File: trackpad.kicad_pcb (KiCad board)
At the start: 2 copper layers, 172 x 152.9 mm, 102 parts, among them J1 USB_C_Receptacle_USB2.0, J10 Conn_01x01_Pin, J3 Conn_01x03, J5 Conn_01x07_Pin, J6 Conn_01x04_Pin, J7 Conn_01x02_Pin, J8 Conn_01x08_Pin, J9 Conn_01x02_Pin, SW1 RotaryEncoder_Switch, SW2 SW_Push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

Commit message: Cleanup
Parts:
- removed R16: 0k, Resistor_SMD:R_0402_1005Metric_Pad0.72x0.64mm_HandSolder
- JP1: footprint Jumper:SolderJumper-3_P1.3mm_Open_RoundedPad1.0x1.5mm -> Jumper:SolderJumper-3_P1.3mm_Bridged2Bar12_RoundedPad1.0x1.5mm
- moved R12 0.66 mm to (95.8, 167.6)
- moved C39 0.19 mm to (96.8, 179.0)
- moved C28 0.19 mm to (100.5, 176.3)
- moved U5 0.15 mm to (98.0, 176.8)
- moved J10 0.14 mm to (101.6, 178.3)
- moved C19 0.12 mm to (108.3, 164.6)
- moved C21 0.12 mm to (108.6, 173.4)
- moved C18 0.11 mm to (108.3, 163.7)
- moved C20 0.10 mm to (107.7, 173.4)
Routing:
- net /Sensor/Shield: track 664.8 -> 672.5 mm
- net VCC: track 87.8 -> 86.3 mm
- net +3V3: track 89.7 -> 88.5 mm
- net Net-(U4-TEST): track 6.34 -> 5.79 mm
- net GND2: track 65.1 -> 65.4 mm, vias 72 -> 71
- net GND: vias 60 -> 63
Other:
- board text added: "RESET"
- board text removed: "Remove R16 first!"
- board text removed: "Reset"

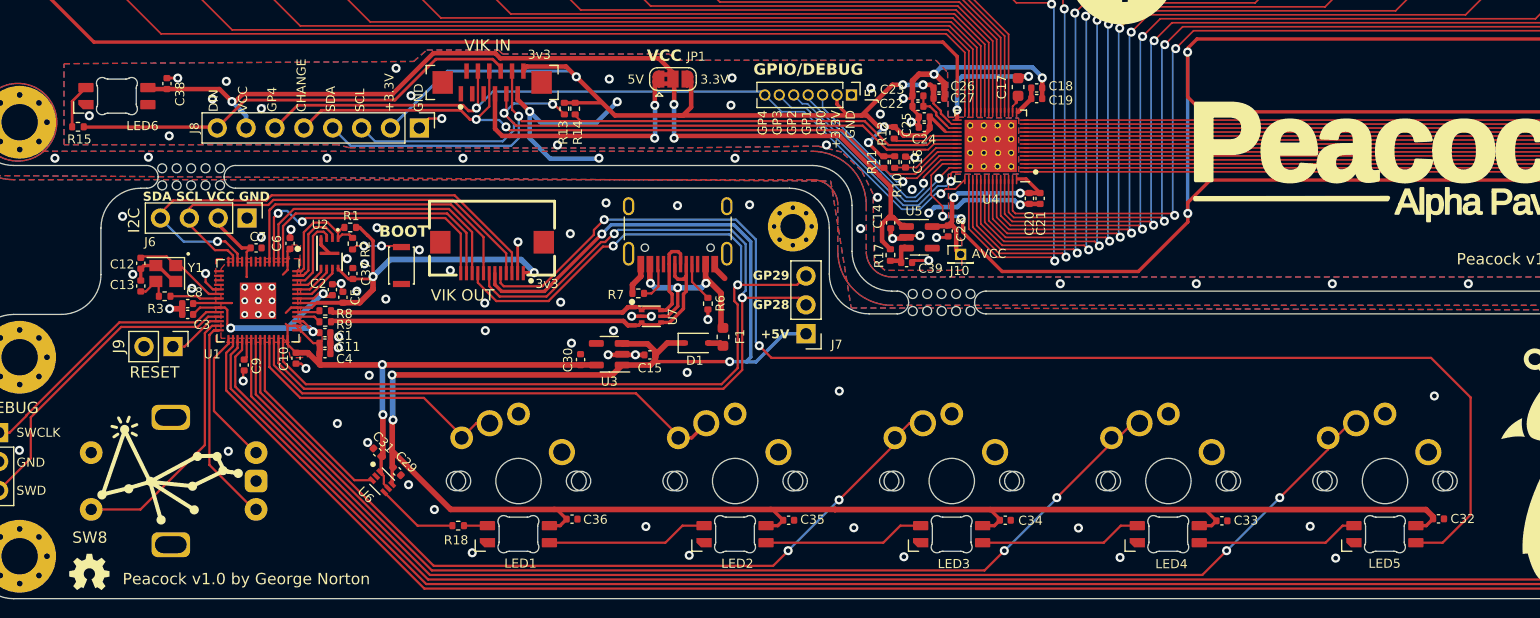
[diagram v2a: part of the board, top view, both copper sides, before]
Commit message: I2C pins were incorrect.
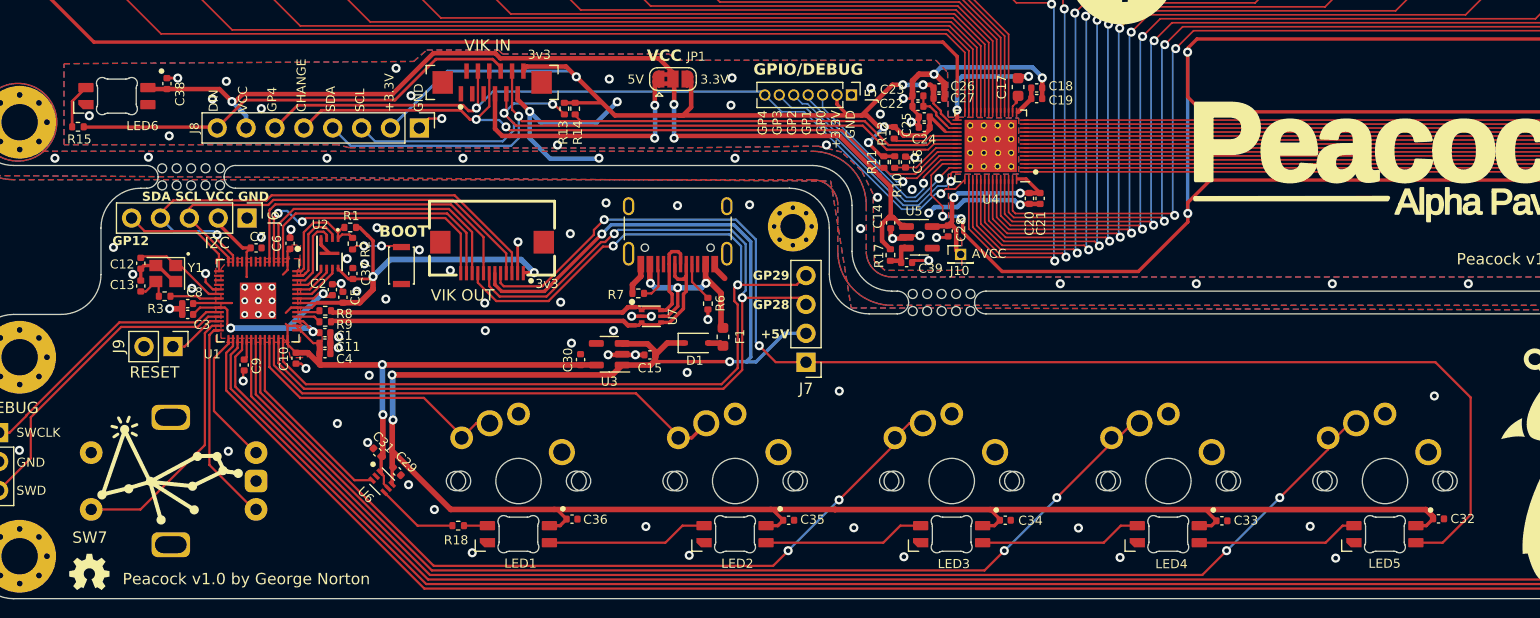
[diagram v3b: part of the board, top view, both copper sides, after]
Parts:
- J6: value Conn_01x04_Pin -> Conn_01x05_Pin; footprint Connector_PinHeader_2.54mm:PinHeader_1x04_P2.54mm_Vertical -> Connector_PinHeader_2.54mm:PinHeader_1x05_P2.54mm_Vertical
- J7: value Conn_01x02_Pin -> Conn_01x04_Pin; footprint Connector_PinHeader_2.54mm:PinHeader_1x03_P2.54mm_Vertical -> Connector_PinHeader_2.54mm:PinHeader_1x04_P2.54mm_Vertical
- U6: footprint Package_TO_SOT_SMD:SOT-563 -> Trackpad:SN74LVC1T45DRLR
- moved J7 2.50 mm to (88.0, 187.8)
- renumbered SW8 to SW7
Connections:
- net /Macropad/SW8 renamed /Macropad/SW7
- J7 pad 1: +5V -> /Macropad/VIK_RGB
- J7 pad 2: /Macropad/GPIO_AD1 -> +5V
- J7 pad 3: /Macropad/GPIO_AD2 -> /Macropad/GPIO_AD1
- U1 pad 12: /Macropad/SDA -> unconnected-(U1-GPIO9-Pad12)
- U1 pad 13: /Macropad/SCL -> /Macropad/SDA
- U1 pad 14: unconnected-(U1-GPIO11-Pad14) -> /Macropad/SCL
- U1 pad 15: unconnected-(U1-GPIO12-Pad15) -> /Macropad/GP12
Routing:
- net /Macropad/GP12: track 0.00 -> 10.5 mm
- net /Macropad/SCL: track 38.8 -> 38.0 mm
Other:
- board text added: "GP12"
- board text added: "SW7"
- board text removed: "SW8"
